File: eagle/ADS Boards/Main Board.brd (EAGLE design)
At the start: 69.8 x 69.8 mm, 14 parts

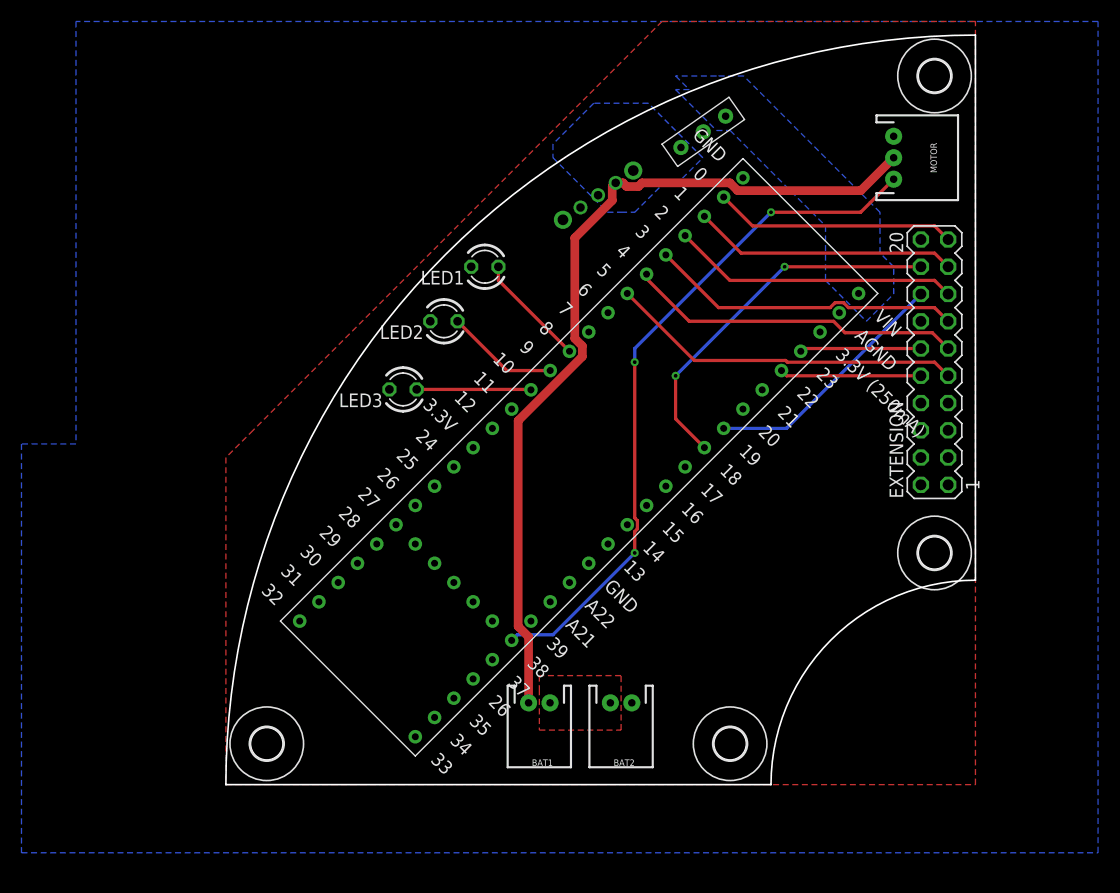
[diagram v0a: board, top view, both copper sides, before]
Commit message: Modify to surface mount components
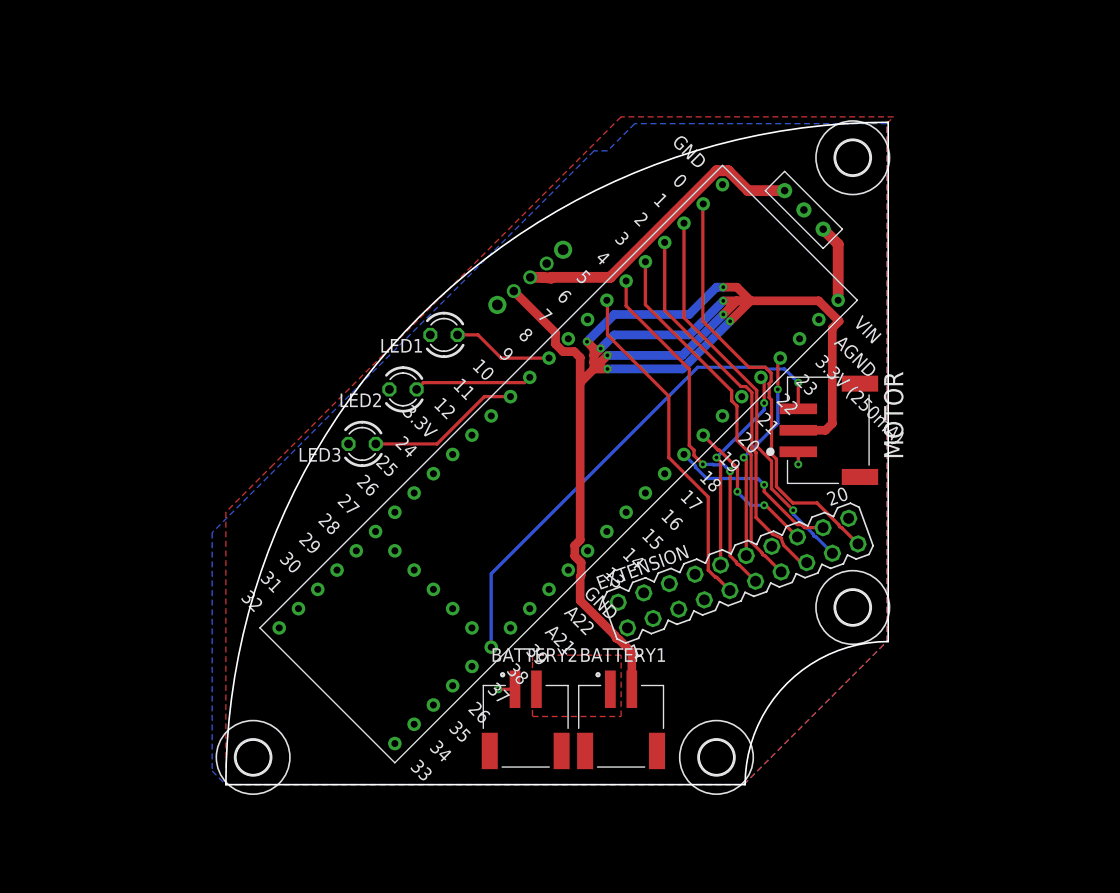
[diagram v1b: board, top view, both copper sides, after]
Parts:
- removed BAT1, BAT2: (no value), SparkFun-Connectors:JST-2-PTH
- added BATTERY1, BATTERY2: S2B-PH-SM4-TB(LF)(SN), S2B-PH-SM4-TB_LF__SN_:JST_S2B-PH-SM4-TB(LF)(SN)
- H1, H2, H3, H4: value MOUNT-HOLE3.0 -> MOUNT-HOLE3.2; device holes:3,0 -> holes:3,2
- MOTOR: value (none) -> S3B-PH-SM4-TB(LF)(SN); device SparkFun-Connectors:JST-3-PTH -> S3B-PH-SM4-TB_LF__SN_:JST_S3B-PH-SM4-TB(LF)(SN)
- moved MOTOR 26.9 mm to (53.3, 33.0)
- moved EXTENSION 26.9 mm to (47.7, 19.7), turned to 20 degrees
- moved U$2 11.7 mm to (52.1, 57.1), turned to 225 degrees
- moved H4 10.8 mm to (58.4, 58.4)
- moved U$3 9.93 mm to (28.4, 47.3), turned to 220 degrees
- moved H3 9.16 mm to (58.4, 16.5)
- moved LED1 7.41 mm to (20.3, 41.9)
- moved LED2 7.41 mm to (16.5, 36.8)
- moved LED3 6.35 mm to (12.7, 31.8)
- moved U$1 2.01 mm to (3.17, 14.6)
- moved H2 1.80 mm to (45.7, 2.54)
- moved H1 1.80 mm to (2.54, 2.54)
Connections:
- net GND: now also BATTERY2.1, U$3.OUT1; no longer BAT2.1, U$3.OUT2
- net N$2: now also BATTERY1.1, BATTERY2.2; no longer BAT1.1, BAT2.2
- net V_BATT: now also BATTERY1.2, U$3.OUT2; no longer BAT1.2, U$3.OUT1
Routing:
- net V_BATT: track 81.3 -> 137.2 mm, vias 0 -> 8
- net V_IN: track 0.00 -> 28.6 mm
- net SDA: track 34.9 -> 16.2 mm, vias 2 -> 1
- net MOTOR: track 64.8 -> 46.5 mm, vias 3 -> 1
- net B1: track 22.6 -> 40.1 mm
- net B2: track 24.7 -> 36.5 mm, vias 0 -> 1
- net SCL: track 23.6 -> 14.0 mm, vias 0 -> 2
- net B3: track 26.8 -> 36.0 mm
- net RST: track 11.3 -> 19.9 mm, vias 0 -> 2
- net 5V: track 0.00 -> 7.20 mm
- net ADR: track 13.2 -> 19.6 mm, vias 0 -> 2
- net B4: track 29.3 -> 34.2 mm
- net ERROR_LED: track 10.7 -> 14.4 mm
- net B5: track 31.2 -> 34.2 mm, vias 0 -> 2
- net GND: track 0.00 -> 2.72 mm, vias 0 -> 2
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- removed copper zone on layer 16, net 5V
- removed copper zone on layer 16, net V_IN
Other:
- board size 69.8 x 69.8 mm -> 61.7 x 61.7 mm

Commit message: Add files via upload
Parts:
- added C1: 0.33µF, SparkFun-Capacitors:0805
- added C2: 0.1uF, SparkFun-Capacitors:0603
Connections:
- net 5V: now also C2.1
- net GND: now also C1.2, C2.2
- net V_IN: now also C1.1
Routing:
- net V_IN: track 28.6 -> 25.2 mm
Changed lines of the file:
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@@
 <?xml version="1.0" encoding="utf-8"?>
 <!DOCTYPE eagle SYSTEM "eagle.dtd">
-<eagle version="9.2.2">
+<eagle version="9.1.3">
 <drawing>
 <settings>
@@
 <attribute name="VALUE" x="48.184790625" y="38.375409375" size="1.7798" layer="27" rot="R270"/>
 </element>
+<element name="C1" library="SparkFun-Capacitors" package="0805" value="0.33µF" x="0.635" y="-3.81">
+<attribute name="PROD_ID" value="CAP-08469" x="0.635" y="-3.81" size="1.778" layer="27" display="off"/>
+</element>
+<element name="C2" library="SparkFun-Capacitors" package="0603" value="0.1uF" x="0.635" y="-7.62">
+<attribute name="PROD_ID" value="CAP-08604" x="0.635" y="-7.62" size="1.778" layer="27" display="off"/>
+</element>
 </elements>
 <signals>
@@
 <via x="53.34" y="29.845" extent="1-16" drill="0.35"/>
 <contactref element="U$3" pad="OUT1"/>
+<contactref element="C1" pad="2"/>
+<contactref element="C2" pad="2"/>
+<wire x1="46.280228125" y1="55.914178125" x2="53.86605" y2="53.557896875" width="0" layer="19" extent="1-1"/>
+<wire x1="29.895821875" y1="48.560753125" x2="46.280228125" y2="55.914178125" width="0" layer="19" extent="1-1"/>
+<wire x1="19.05" y1="41.91" x2="29.895821875" y2="48.560753125" width="0" layer="19" extent="1-1"/>
+<wire x1="15.24" y1="36.83" x2="19.05" y2="41.91" width="0" layer="19" extent="1-1"/>
+<wire x1="11.43" y1="31.75" x2="15.24" y2="36.83" width="0" layer="19" extent="1-1"/>
+<wire x1="19.339459375" y1="18.1971" x2="11.43" y2="31.75" width="0" layer="19" extent="1-1"/>
+<wire x1="25.4" y1="8.89" x2="19.339459375" y2="18.1971" width="0" layer="19" extent="1-1"/>
+<wire x1="37.425596875" y1="14.61095" x2="26.94" y2="8.89" width="0" layer="19" extent="1-1"/>
+<wire x1="31.91181875" y1="19.993153125" x2="37.425596875" y2="14.61095" width="0" layer="19" extent="1-1"/>
+<wire x1="53.34" y1="29.845" x2="37.425596875" y2="14.61095" width="0" layer="19" extent="1-1"/>
+<wire x1="1.535" y1="-3.81" x2="25.4" y2="8.89" width="0" layer="19" extent="1-1"/>
+<wire x1="1.485" y1="-7.62" x2="1.535" y2="-3.81" width="0" layer="19" extent="1-1"/>
 </signal>
 <signal name="3.3V">
@@
 <wire x1="55.6621" y1="51.76184375" x2="57.056534375" y2="50.367409375" width="1.016" layer="1"/>
 <wire x1="57.056534375" y1="50.367409375" x2="57.056534375" y2="45.13786875" width="1.016" layer="1"/>
+<contactref element="C2" pad="1"/>
+<wire x1="-0.215" y1="-7.62" x2="57.056534375" y2="45.13786875" width="0" layer="19" extent="1-1"/>
 </signal>
 <signal name="V_BATT">
@@
 <signal name="V_IN">
 <contactref element="U$3" pad="IN"/>
-<contactref element="U$2" pad="INPUT"/>
 <wire x1="28.363734375" y1="47.275178125" x2="29.508853125" y2="47.275178125" width="1.016" layer="1"/>
 <wire x1="29.508853125" y1="47.275178125" x2="30.3236375" y2="47.20389375" width="1.016" layer="1"/>
@@
 <wire x1="35.809253125" y1="47.275178125" x2="45.743659375" y2="57.209584375" width="1.016" layer="1"/>
 <wire x1="46.81680625" y1="57.209584375" x2="48.67244375" y2="55.353946875" width="1.016" layer="1"/>
-<wire x1="48.67244375" y1="55.353946875" x2="52.07" y2="55.353946875" width="1.016" layer="1"/>
+<contactref element="C1" pad="1"/>
+<contactref element="U$2" pad="INPUT"/>
+<wire x1="48.67244375" y1="55.353946875" x2="52.07" y2="55.353946875" width="0" layer="19" extent="1-1"/>
+<wire x1="-0.265" y1="-3.81" x2="28.363734375" y2="47.275178125" width="0" layer="19" extent="1-1"/>
 </signal>
 <signal name="MOTOR">
